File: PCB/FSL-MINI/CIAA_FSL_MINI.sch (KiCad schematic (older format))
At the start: 12 parts

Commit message: Primer recorte realizado con Esteban Volentini <evolentini@gmail.com>.
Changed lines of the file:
@@
 $Descr A4 11693 8268
 encoding utf-8
-Sheet 1 13
+Sheet 1 6
 Title "CIAA Freescale MINI - Esquemático jerárquico"
 Date "2016-06-01"
 Rev "CORDOBA 0.1"
 Comp "CIAA - COMPUTADORA INDUSTRIAL ABIERTA ARGENTINA. Versión FSL-MINI (K60)"
-Comment1 "Autores: Ver 'doc/CHANGES.txt'      Licencia: Ver  'doc/LICENCIA_CIAA_FSL.txt'"
+Comment1 "Autores: Ver 'doc/CHANGES.txt'      Licencia: Ver  'doc/LICENCIA.txt'"
 Comment2 ""
 Comment3 ""
@@
 $EndSheet
 $Sheet
-S 5800 4000 1150 1200
-U 52C1F703
-F0 "RS485_RS232_CAN" 50
-F1 "rsS485_rs232_can.sch" 50
-F2 "RS485_RXD" O L 5800 5100 60
-F3 "RS485_DIR" I L 5800 4900 60
-F4 "RS485_TXD" I L 5800 5000 60
-F5 "RS232_RXD" O L 5800 4550 60
-F6 "RS232_TXD" I L 5800 4450 60
-F7 "RS232_RTS" I L 5800 4650 60
-F8 "RS232_CTS" O L 5800 4750 60
-F9 "CAN_TD" I L 5800 4200 60
-F10 "CAN_RD" O L 5800 4100 60
-F11 "CAN_STB" I L 5800 4300 60
-$EndSheet
-$Sheet
 S 5800 5350 1150 800
 U 52C66C60
@@
 F6 "USB0_PPWR" I L 5800 5850 60
 F7 "USB0_PWR_FAULT" O L 5800 5950 60
-$EndSheet
-$Sheet
-S 900  850  1250 3500
-U 52CA0F12
-F0 "GPIO" 50
-F1 "gpio.sch" 50
-F2 "GPIO0" B R 2150 950 60
-F3 "GPIO2" B R 2150 1150 60
-F4 "GPIO4" B R 2150 1350 60
-F5 "GPIO6" B R 2150 1550 60
-F6 "GPIO8" B R 2150 1750 60
-F7 "GPIO10" B R 2150 1950 60
-F8 "GPIO12" B R 2150 2150 60
-F9 "GPIO14" B R 2150 2350 60
-F10 "GPIO1" B R 2150 1050 60
-F11 "GPIO3" B R 2150 1250 60
-F12 "GPIO5" B R 2150 1450 60
-F13 "GPIO7" B R 2150 1650 60
-F14 "GPIO9" B R 2150 1850 60
-F15 "GPIO11" B R 2150 2050 60
-F16 "GPIO13" B R 2150 2250 60
-F17 "GPIO15" B R 2150 2450 60
-F18 "I2C_SDA" B R 2150 2800 60
-F19 "I2C_SCL" I R 2150 2900 60
-F20 "AN0" O R 2150 3250 60
-F21 "AN1" O R 2150 3350 60
-F22 "AN2" O R 2150 3450 60
-F23 "AN3" O R 2150 3550 60
-F24 "AUX_UART_RX/SPI_MISO" O R 2150 4100 60
-F25 "AUX_UART_TX/SPI_MOSI" I R 2150 4200 60
-F26 "AUX_UART_CTS/SPI_CLK" I R 2150 4000 60
-F27 "AUX_UART_RTS/SPI_CS" I R 2150 3900 60
-$EndSheet
-$Sheet
-S 900  4550 1250 900
-U 52CA388F
-F0 "Entradas Digitales" 50
-F1 "din.sch" 50
-F2 "DIN0" O R 2150 4650 60
-F3 "DIN1" O R 2150 4750 60
-F4 "DIN2" O R 2150 4850 60
-F5 "DIN3" O R 2150 4950 60
-F6 "DIN4" O R 2150 5050 60
-F7 "DIN5" O R 2150 5150 60
-F8 "DIN6" O R 2150 5250 60
-F9 "DIN7" O R 2150 5350 60
-$EndSheet
-$Sheet
-S 900  5600 1250 900
-U 52CC00C6
-F0 "Salidas Digitales" 50
-F1 "dout.sch" 50
-F2 "DOUT1" I R 2150 5800 60
-F3 "DOUT3" I R 2150 6000 60
-F4 "DOUT0" I R 2150 5700 60
-F5 "DOUT2" I R 2150 5900 60
-F6 "DOUT4" I R 2150 6100 60
-F7 "DOUT5" I R 2150 6200 60
-F8 "DOUT6" I R 2150 6300 60
-F9 "DOUT7" I R 2150 6400 60
-$EndSheet
-$Sheet
-S 5800 6300 1150 500
-U 52C8476B
-F0 "Ent. Analógicas" 50
-F1 "analog.sch" 50
-F2 "AIN0" O L 5800 6400 60
-F3 "AIN1" O L 5800 6500 60
-F4 "AIN2" O L 5800 6600 60
-F5 "AIN3" O L 5800 6700 60
 $EndSheet
 $Sheet
@@
 F4 "VBAT" O R 9750 4300 60
 $EndSheet
-$Sheet
-S 5800 6950 1150 500
-U 5340ACAE
-F0 "Salida Analogica" 50
-F1 "analog_out.sch" 50
-F2 "DAC_OUT" I L 5800 7200 60
-$EndSheet
-$Sheet
-S 900  6650 1250 950
-U 5386CF75
-F0 "JTAG" 50
-F1 "JTAG.sch" 50
-F2 "USB_DEBUG_VBUS" O R 2150 7050 60
-F3 "USB_JTAG_UART_RXD" O R 2150 6750 60
-F4 "USB_JTAG_UART_TXD" I R 2150 6850 60
-F5 "TCK" O R 2150 7300 60
-F6 "TDI" O R 2150 7500 60
-F7 "TDO" I R 2150 7400 60
-F8 "TMS" O R 2150 7200 60
-F9 "RESET" O R 2150 6950 60
-$EndSheet
 Text Notes 7800 3700 0    118  ~ 0

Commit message: Added temporal connectors to avoid ERC.
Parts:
- added P101, P102: CONN_02X18, symbol CONN_02X18
- added P103: CONN_01X05, symbol CONN_01X05
- renumbered F1 to F101, F2 to F102, F3 to F103, F4 to F104, F5 to F105, F6 to F106, G102 to G101, G101 to G102, H1 to H101, H2 to H102, H3 to H103, H4 to H104
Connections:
- net labels added: CON5V, CONBAT, GND
- net labels removed: I2C_SCL, I2C_SDA, RESET, USB_DEBUG_VBUS
- wire segments 106 -> 194
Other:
- note added: "Computadora Industrial Abierta Argentina\nVersión FSL-MINI (K60)"
- note added: "NOTAS DESARROLLO:\n1)Los conectores y su conexionado es provisorio\nfalta estudiar como distribuir las señales y cuales \nusar.\n2) No se borraron señales salientes de la jerarquía\nde la CPU."
- note added: "Índice:\n1. Esquemático jerárquico\n2. Ethernet\n3. USB OTG\n4. Memorias NV\n5. Fuente de alimentación\n6. CPU\n\n\n\n"
- note removed: "Computadora Industrial Abierta Argentina\nVersión FSL-MINI (Freescale K60)"
- note removed: "Índice:\n1. Esquemático jerárquico\n2. CPU\n3. Ethernet\n4. RS485/RS232/CAN\n5. USB OTG\n6. GPIO\n7. Entradas digitales\n8. Salidas digitales\n9. Entradas analógicas\n10. Memorias NV\n11. Fuente de alimentación\n12. Salida Analogica\n13. JTAG\n"
- moved on the sheet: F101, F102, F103, F104, F105, F106, H101, H102, H103, H104

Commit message: Footprint information in schematics.
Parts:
- F101, F102, F103, F104, F105, F106: footprint Fiducial_1mm -> footprints:Fiducial_1mm
- G101: footprint LOGO-CIAA -> footprints:LOGO-CIAA
- G102: footprint OSHWA -> footprints:OSHWA
- H101, H102, H103, H104: footprint PCB_HOLE -> footprints:PCB_HOLE
- P101, P102: value CONN_02X18 -> CONN_02X17; footprint (none) -> Pin_Headers:Pin_Header_Straight_2x17_Pitch2.00mm; symbol CONN_02X18 -> CONN_02X17
- P103: footprint (none) -> Pin_Headers:Pin_Header_Straight_1x05
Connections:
- wire segments 194 -> 192

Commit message: Agregada hoja con conectores de entradas/salidas.  Las pineras reemplazan a las del commit anterior. Ambas pineras poseen las mismas líneas asignadas que las pineras eliminidas, pero sin respetar la misma distribución pin a pin.
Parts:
- removed P101, P102: CONN_02X17, Pin_Headers:Pin_Header_Straight_2x17_Pitch2.00mm, symbol CONN_02X17
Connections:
- wire segments 192 -> 127

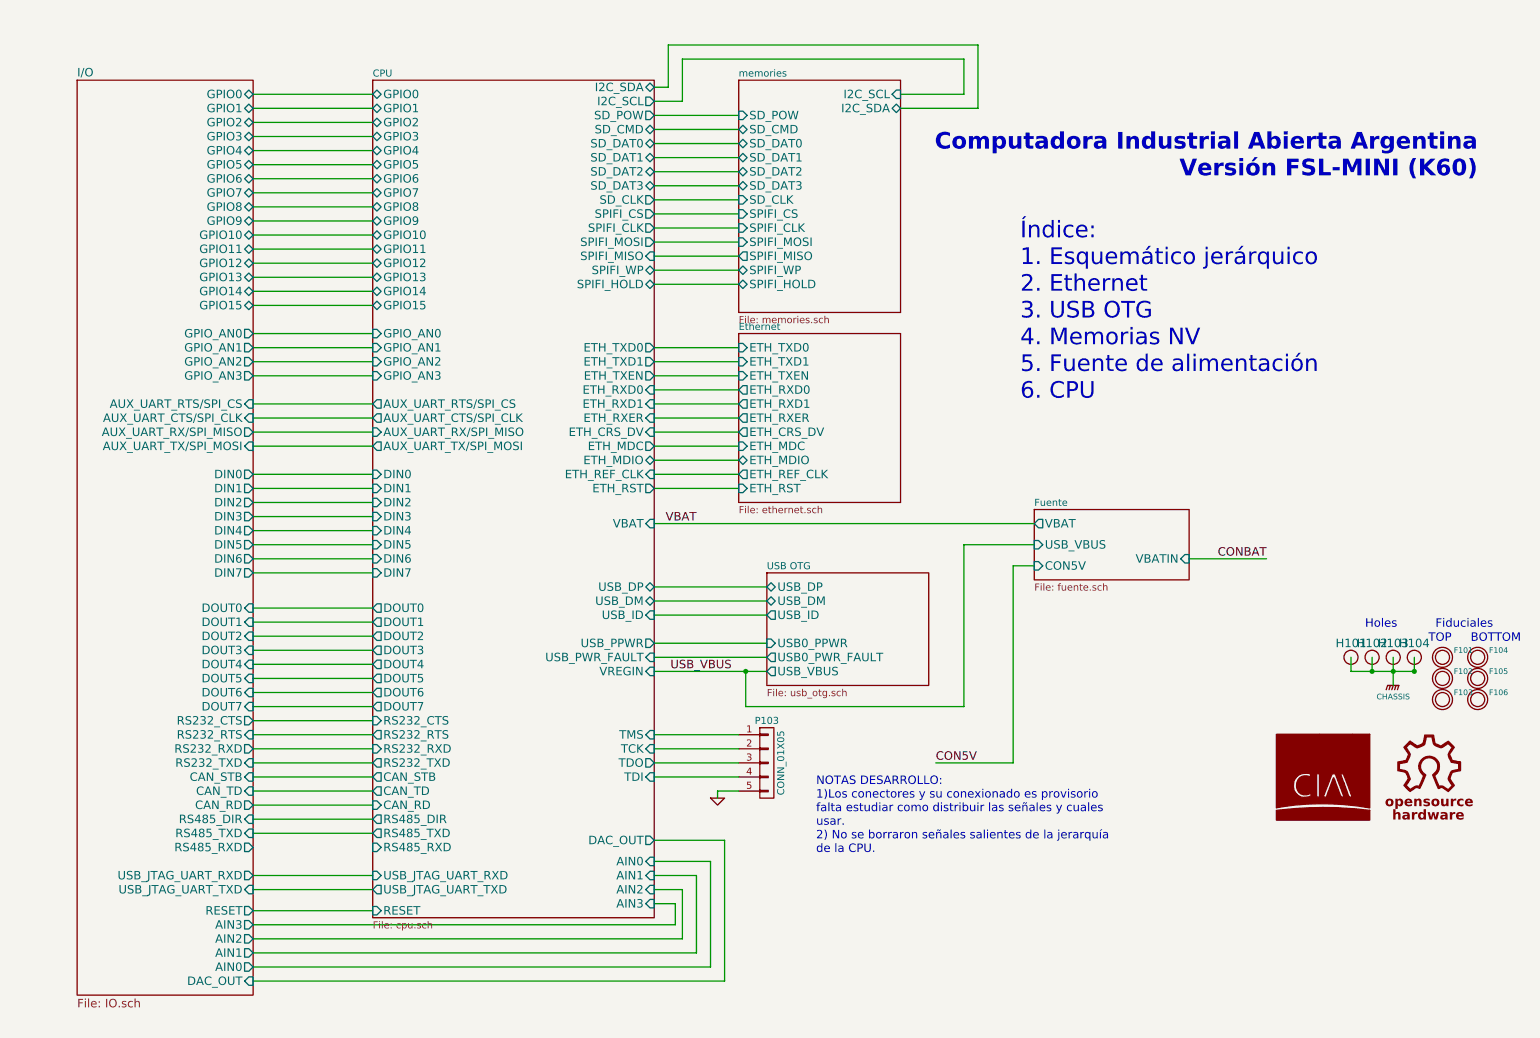
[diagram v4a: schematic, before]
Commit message: Add schematic and PCB component for Arduino UNO shield.  The libraries downloaded from http://meta-blog.eklablog.com/kicad-librairie-arduino-pretty-p930786. Add jumper selector between Arduino VrefH or internal 3.3v. Add level shifter TXB0108.
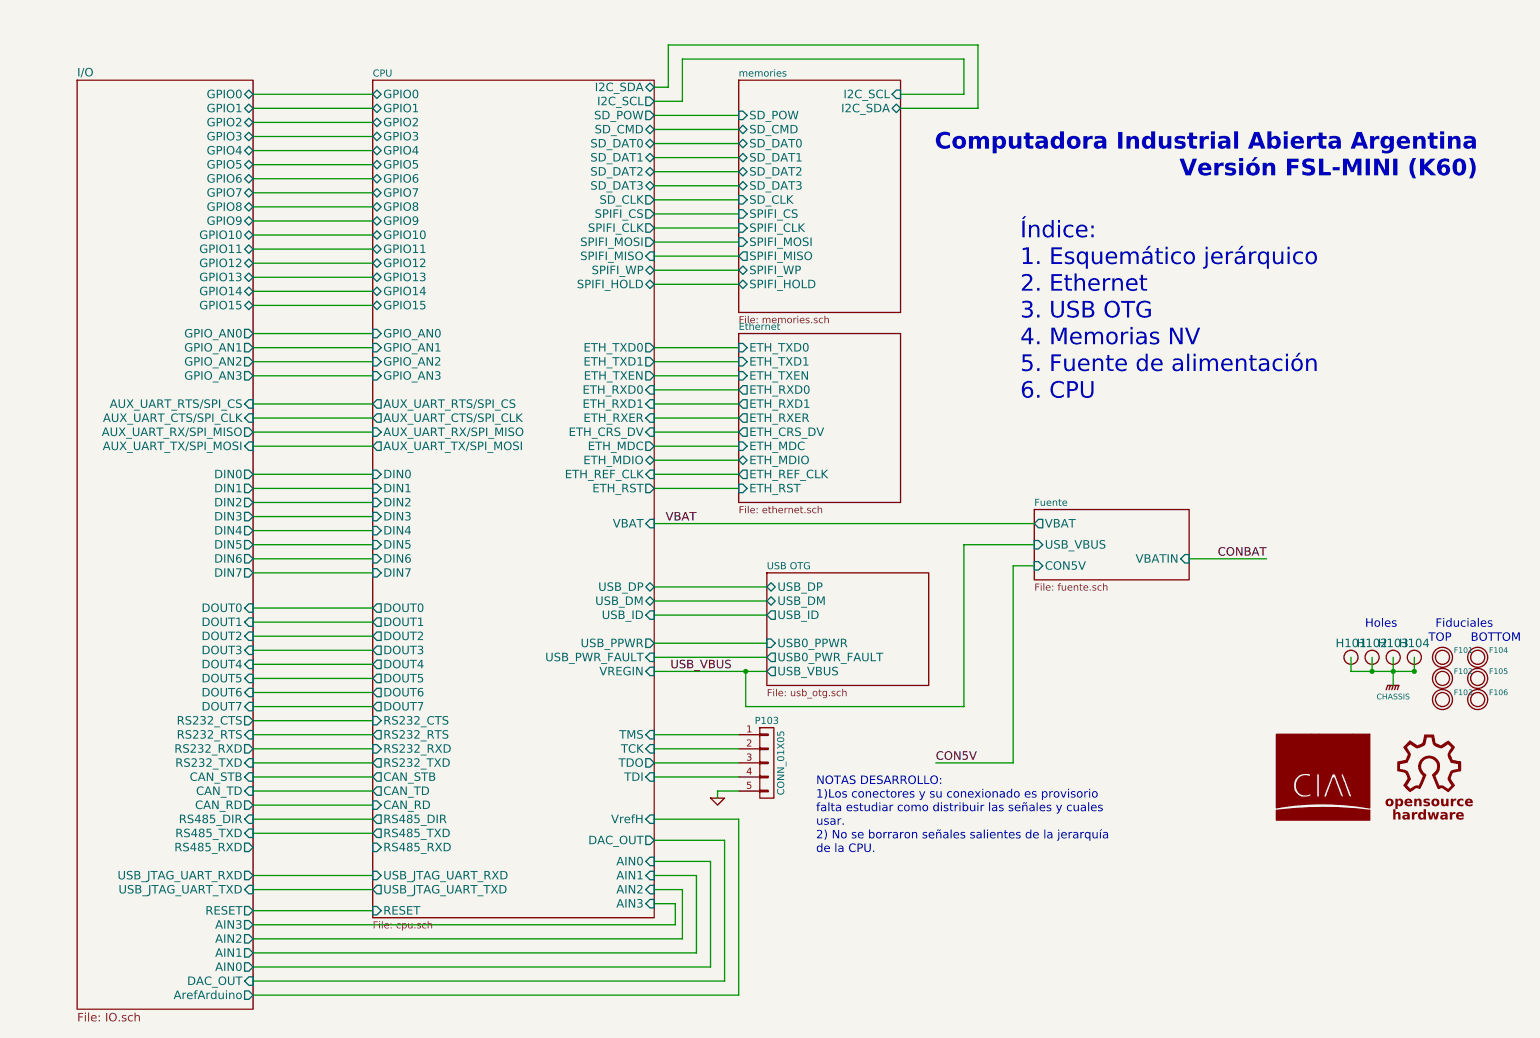
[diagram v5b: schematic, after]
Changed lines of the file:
@@
 EESchema Schematic File Version 2
+LIBS:TXB0108
 LIBS:CIAAK60LIB
 LIBS:conn
+LIBS:shield_arduino
+LIBS:device
 LIBS:CIAA_FSL_MINI-cache
 EELAYER 25 0
@@
 F95 "DAC_OUT" O R 4950 6400 60
 F96 "RESET" I L 2950 6900 60
+F97 "VrefH" I R 4950 6250 60
 $EndSheet
 Text Label 6950 5850 0    60   ~ 0
@@
 NOTAS DESARROLLO:\n1)Los conectores y su conexionado es provisorio\nfalta estudiar como distribuir las señales y cuales \nusar.\n2) No se borraron señales salientes de la jerarquía\nde la CPU.
 $Sheet
-S 850  1000 1250 6500
+S 850  1000 1250 6600
 U 5756CD3E
 F0 "I/O" 60
@@
 F58 "RESET" O R 2100 6900 60
 F59 "DAC_OUT" I R 2100 7400 60
+F60 "ArefArduino" O R 2100 7500 60
 $EndSheet
 Wire Wire Line
@@
 Wire Wire Line
 	5450 7400 5450 6400
+Wire Wire Line
+	2100 7500 5550 7500
+Wire Wire Line
+	5550 7500 5550 6250
+Wire Wire Line
+	5550 6250 4950 6250
 $EndSCHEMATC

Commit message: Correción de lineas entre micro y Arduino. Eliminado TXB0108.  Pinera arduino será solo 3v3 compatible. I2C1 del micro asignado a I2C de Arduino.  Pines I2C de Arduino quedan imposibilitadas como entradas analógicas.
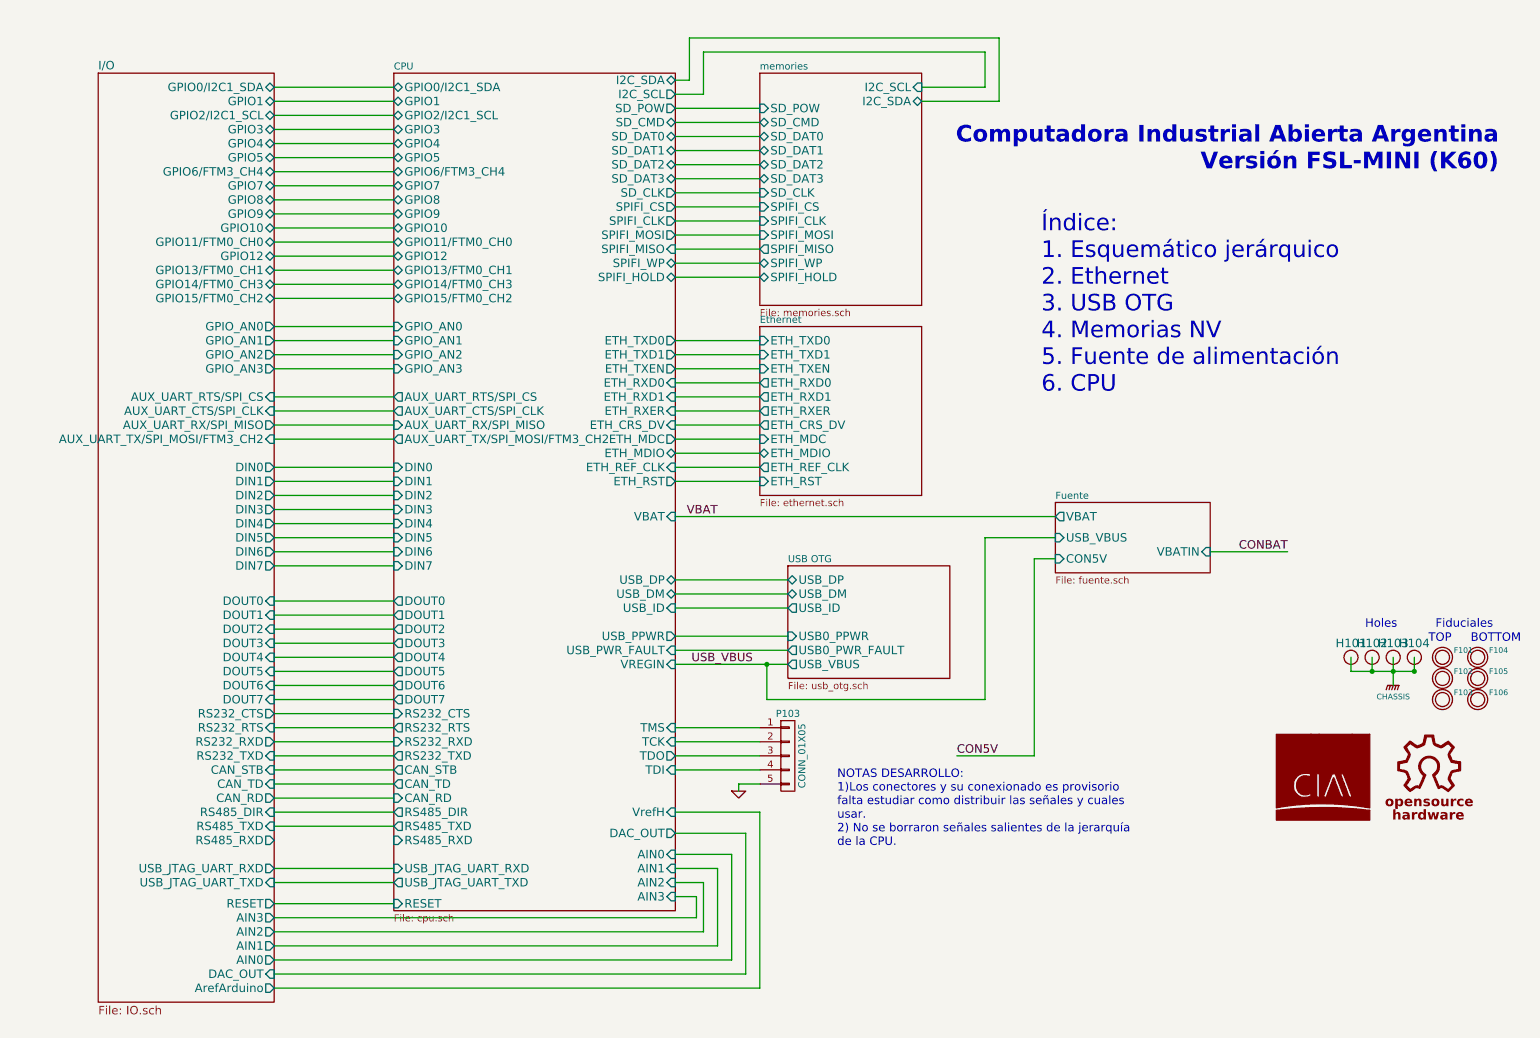
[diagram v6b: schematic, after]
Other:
- moved on the sheet: P103

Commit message: Terminated proposal pin assignment to expansion connector. Correction pinout of general purpose connectors. Correction of CON5v y CONBAT signals.
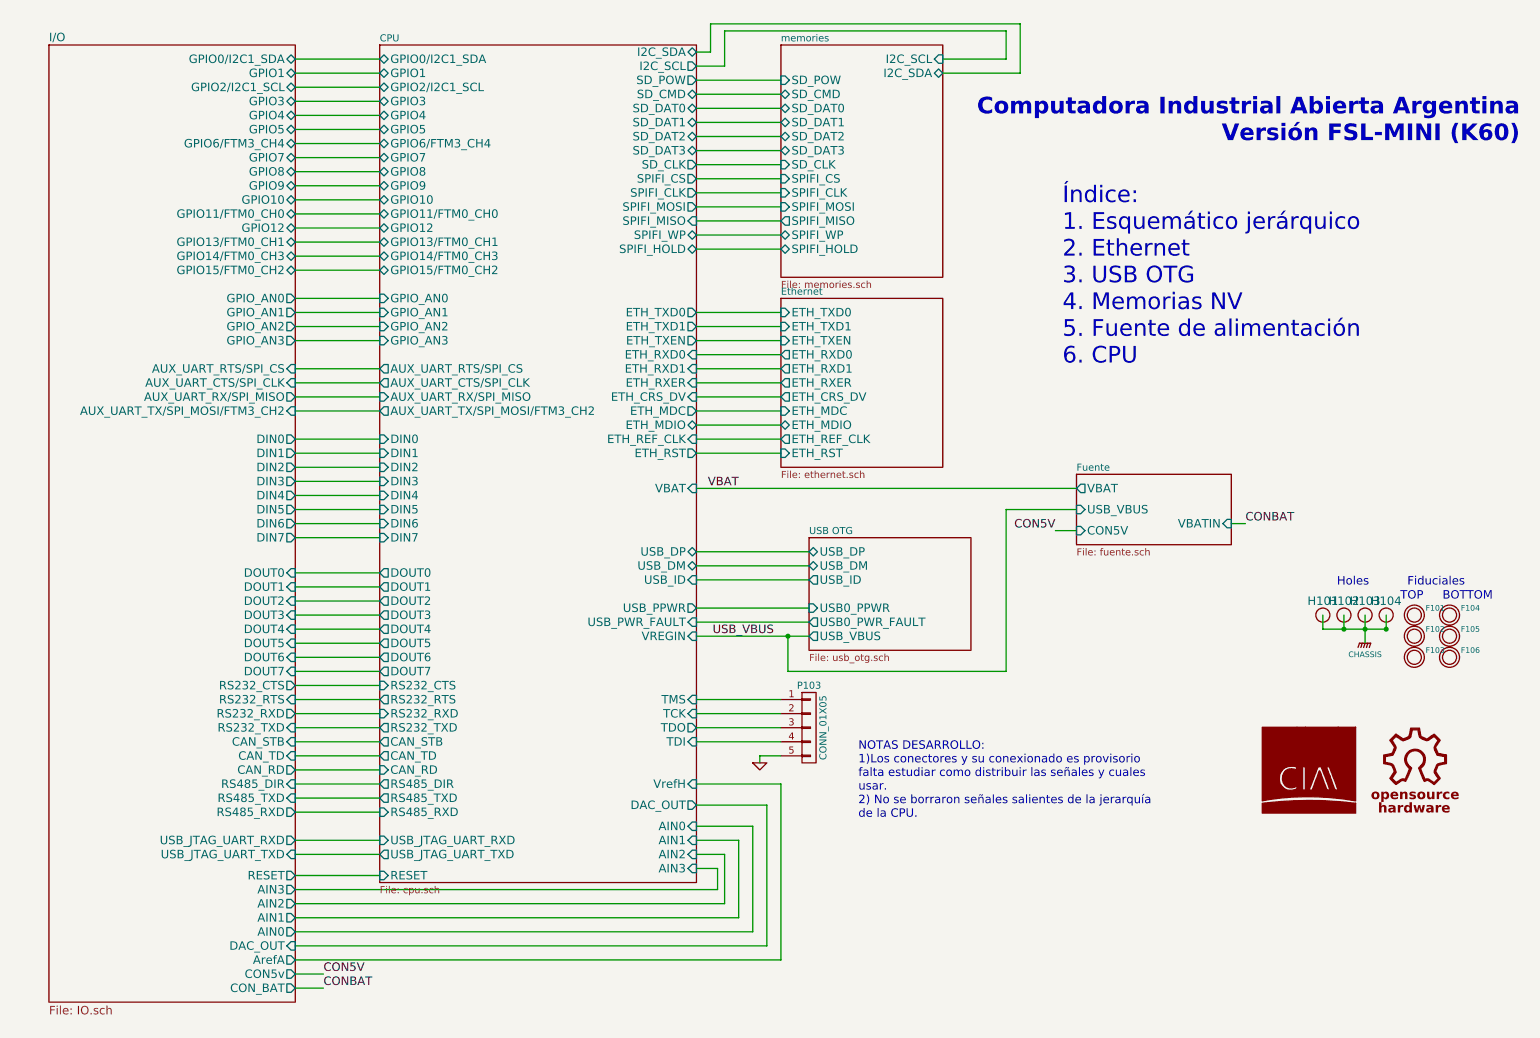
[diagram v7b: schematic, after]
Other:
- moved on the sheet: F101, F102, F103, F104, F105, F106, H101, H102, H103, H104, P103
